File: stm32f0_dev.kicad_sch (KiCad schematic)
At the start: 29 parts, among them U1 STM32F030K6Tx, U2 AP2112K-3.3

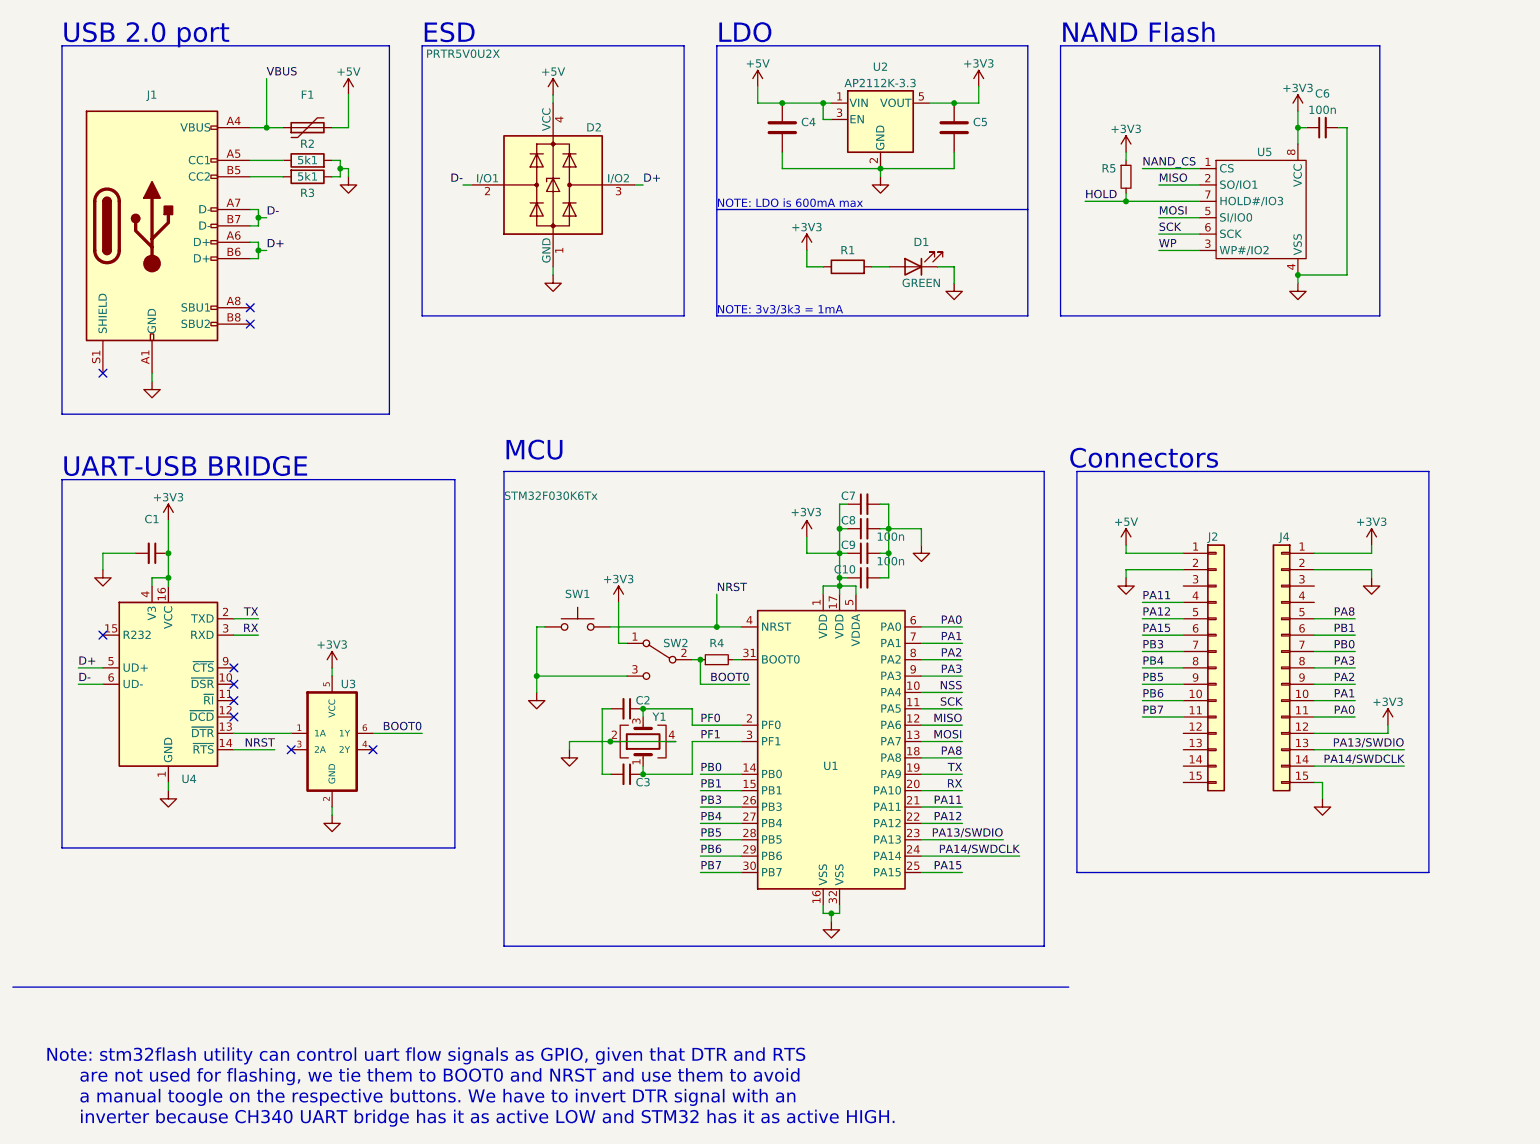
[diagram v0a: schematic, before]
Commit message: Schematic done, routing done, to fix issues on board
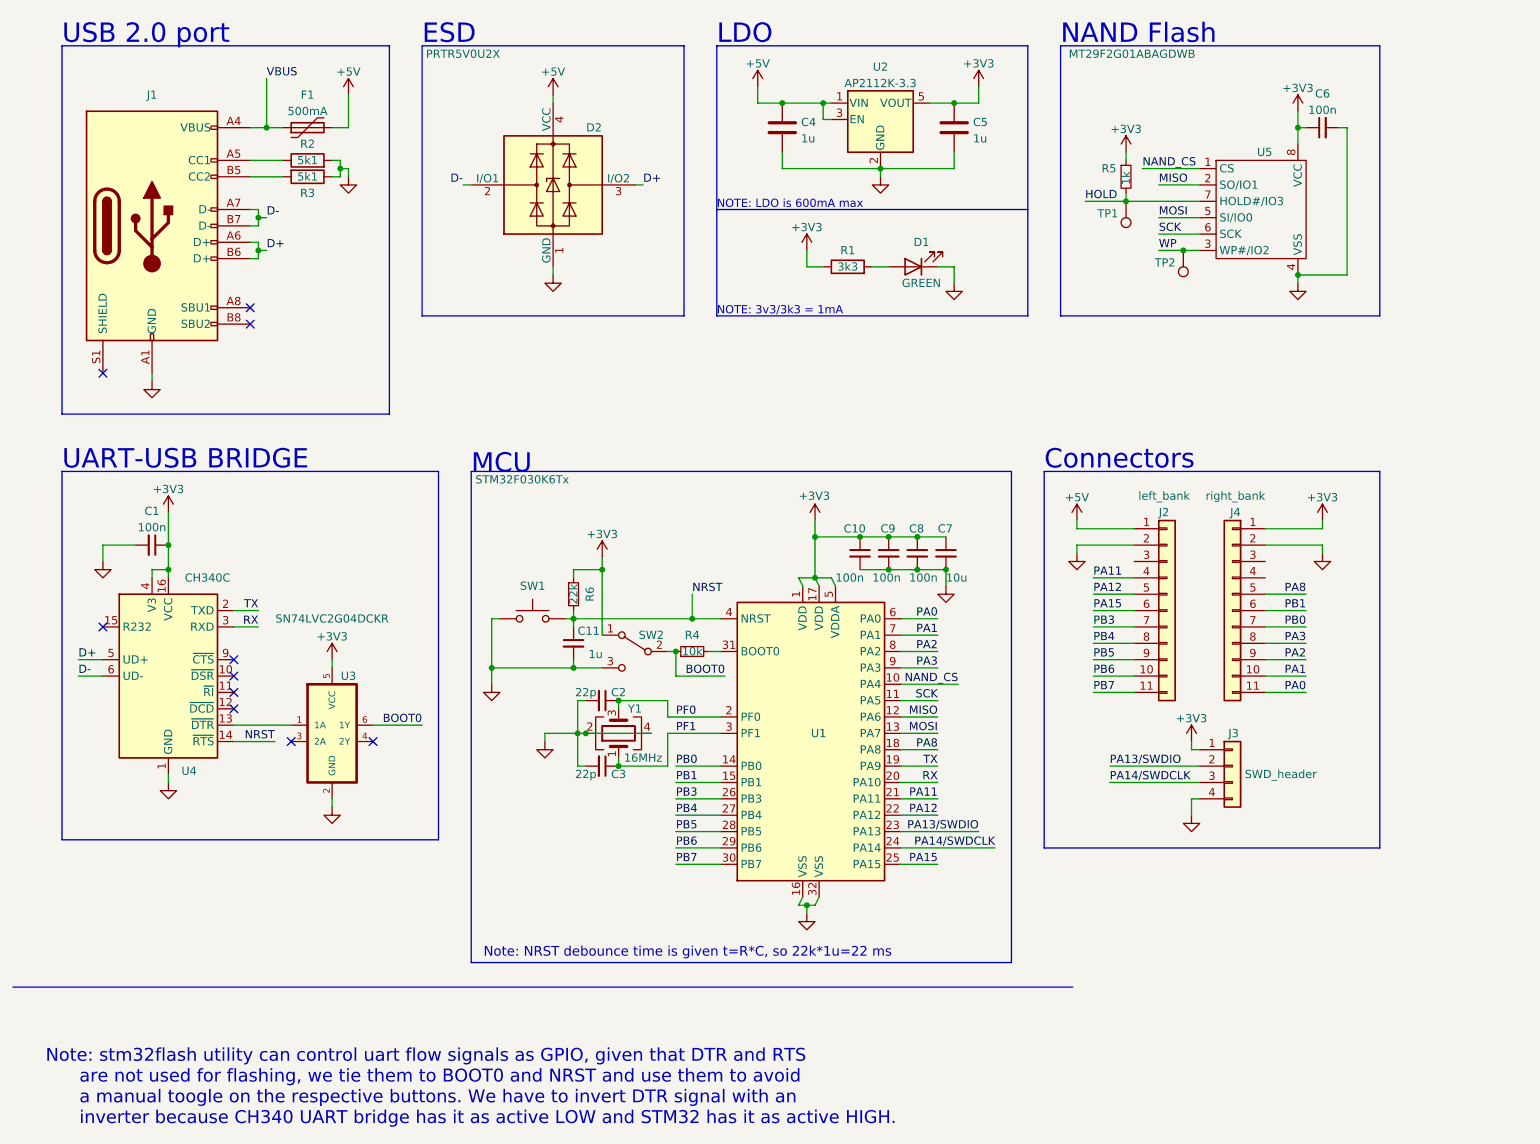
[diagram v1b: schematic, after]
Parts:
- removed J2, J4: (no value), symbol Connector_Generic:Conn_01x15
- added C11: 1u, Capacitor_SMD:C_0603_1608Metric, symbol Device:C_Small
- added J2: left_bank, Connector_PinHeader_2.54mm:PinHeader_1x11_P2.54mm_Vertical, symbol Connector_Generic:Conn_01x11
- added J3: SWD_header, Connector_PinHeader_2.54mm:PinHeader_1x04_P2.54mm_Vertical, symbol Connector_Generic:Conn_01x04
- added J4: right_bank, Connector_PinHeader_2.54mm:PinHeader_1x11_P2.54mm_Vertical, symbol Connector_Generic:Conn_01x11
- added R6: 22k, Resistor_SMD:R_0603_1608Metric, symbol Device:R_Small
- added TP1, TP2: TestPoint, TestPoint:TestPoint_Pad_D1.0mm, symbol Connector:TestPoint
- C1, C10: value (none) -> 100n; footprint (none) -> Capacitor_SMD:C_0603_1608Metric
- C2, C3: value (none) -> 22p; footprint (none) -> Capacitor_SMD:C_0603_1608Metric
- C4, C5: value (none) -> 1u; footprint (none) -> Capacitor_SMD:C_0603_1608Metric
- C6, C8, C9: footprint (none) -> Capacitor_SMD:C_0603_1608Metric
- C7: value (none) -> 10u; footprint (none) -> Capacitor_SMD:C_0603_1608Metric
- D1: footprint (none) -> LED_SMD:LED_0603_1608Metric
- F1: value (none) -> 500mA; footprint (none) -> Fuse:Fuse_0603_1608Metric
- J1: value (none) -> USB_C_Receptacle_USB2.0; footprint (none) -> Connector_USB:USB_C_Receptacle_HRO_TYPE-C-31-M-12
- R1: value (none) -> 3k3; footprint (none) -> Resistor_SMD:R_0603_1608Metric
- R2, R3: footprint (none) -> Resistor_SMD:R_0603_1608Metric
- R4: value (none) -> 10k; footprint (none) -> Resistor_SMD:R_0603_1608Metric
- R5: value (none) -> 1k; footprint (none) -> Resistor_SMD:R_0603_1608Metric
- SW1: value (none) -> SW_Push; footprint (none) -> SKRPACE010:SW_SKRPACE010
- SW2: value (none) -> SW_SPDT; footprint (none) -> SSSS811101 :SSSS811101
- U3: value (none) -> SN74LVC2G04DCKR; footprint (none) -> SN74LVC2G04DCKR:SOT65P210X110-6N
- U4: value (none) -> CH340C; footprint (none) -> Package_SO:SOIC-16_3.9x9.9mm_P1.27mm
- U5: value (none) -> MT29F2G01ABAGDWB; footprint (none) -> MT29F2G01ABAGDWB:SON127P600X800X65-8N
- Y1: value (none) -> 16MHz; footprint (none) -> Crystal:Crystal_SMD_2016-4Pin_2.0x1.6mm
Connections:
- net NSS is gone; now on net NAND_CS: U1.10 (PA4)
- net +3V3: now also J3.1 (Pin_1), J4.1 (Pin_1), R6.1
- net +5V: now also J2.1 (Pin_1)
- net GND: now also C2.2, C3.2, C11.2, J2.2 (Pin_2), J3.4 (Pin_4), J4.2 (Pin_2)
- net HOLD: now also TP1.1
- net NRST: now also C11.1, R6.2
- net PA0: now also J4.11 (Pin_11)
- net PA1: now also J4.10 (Pin_10)
- net PA11: now also J2.4 (Pin_4)
- net PA12: now also J2.5 (Pin_5)
- net PA13/SWDIO: now also J3.2 (Pin_2)
- net PA14/SWDCLK: now also J3.3 (Pin_3)
- net PA15: now also J2.6 (Pin_6)
- net PA2: now also J4.9 (Pin_9)
- net PA3: now also J4.8 (Pin_8)
- net PA8: now also J4.5 (Pin_5)
- net PB0: now also J4.7 (Pin_7)
- net PB1: now also J4.6 (Pin_6)
- net PB3: now also J2.7 (Pin_7)
- net PB4: now also J2.8 (Pin_8)
- net PB5: now also J2.9 (Pin_9)
- net PB6: now also J2.10 (Pin_10)
- net PB7: now also J2.11 (Pin_11)
- net WP: now also TP2.1
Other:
- note added: "Note: NRST debounce time is given t=R*C, so 22k*1u=22 ms"
- moved on the sheet: C1, C10, C2, C3, C7, C8, C9, R4, SW1, SW2, U1, U3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

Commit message: Finished board, added gerber folder, uart leds, board dimensions
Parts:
- added D3, D4: RED, LED_SMD:LED_0603_1608Metric, symbol Device:LED
- added R7, R8: 3k3, Resistor_SMD:R_0603_1608Metric, symbol Device:R
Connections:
- net +3V3: now also R7.1, R8.1
- net RX: now also U4.2 (TXD), D4.1 (K); no longer U4.3 (RXD)
- net TX: now also U4.3 (RXD), D3.1 (K); no longer U4.2 (TXD)
- new net: D4.2 (A), R8.2
- new net: D3.2 (A), R7.2
- no-connect marks 10 -> 13
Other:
- note added: "Note: RX and TX signals are named in respect to mcu, so must be swapped here"
- note added: "Note: stm32flash utility can control uart flow signals as GPIO, given that DTR and RTS are not used for flashing, we tie them to BOOT0 and NRST and use them to avoid manually actuating them for flashing. We have to invert DTR signal with an because CH340 UART bridge has it as active LOW and STM32 has it as active HIGH."
- note added: "Status LEDs"
- note removed: "Note: stm32flash utility can control uart flow signals as GPIO, given that DTR and RTS are not used for flashing, we tie them to BOOT0 and NRST and use them to avoid a manual toogle on the respective buttons. We have to invert DTR signal with an inverter because CH340 UART bridge has it as active LOW and STM32 has it as active HIGH."
- moved on the sheet: C4, C5, C6, D1, R1, R4, R5, TP1, TP2, U2, U5

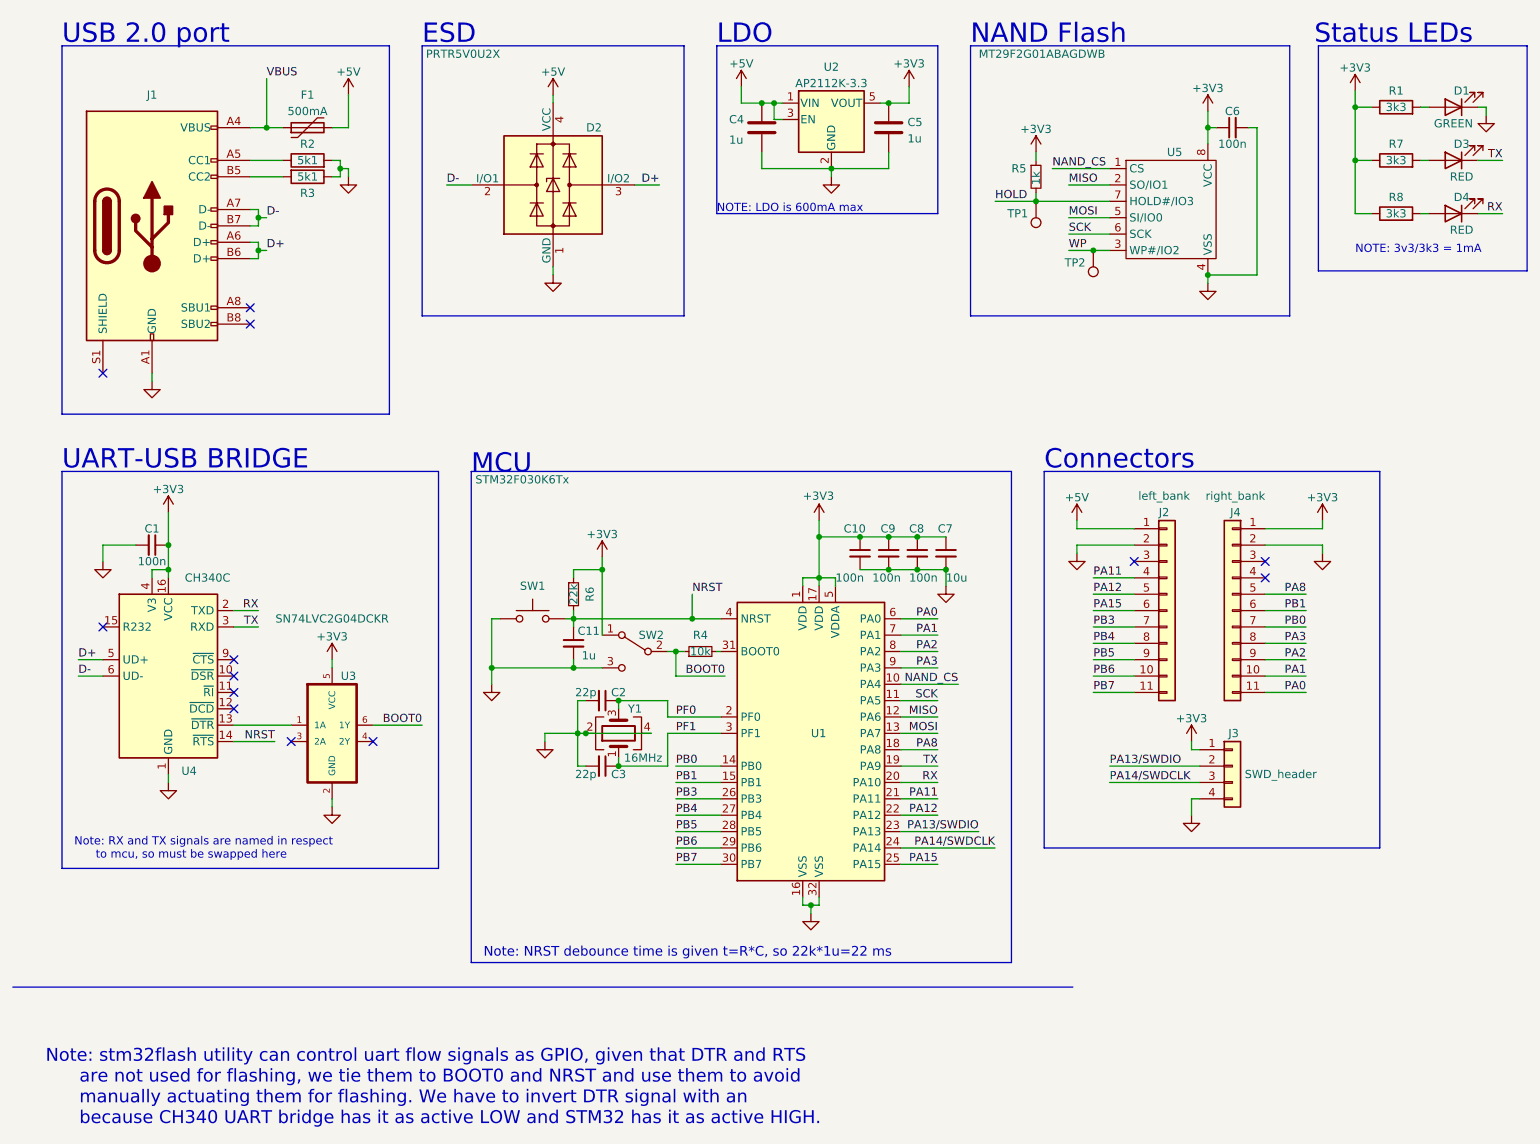
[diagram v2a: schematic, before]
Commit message: Fixed nrst button, dtr signal
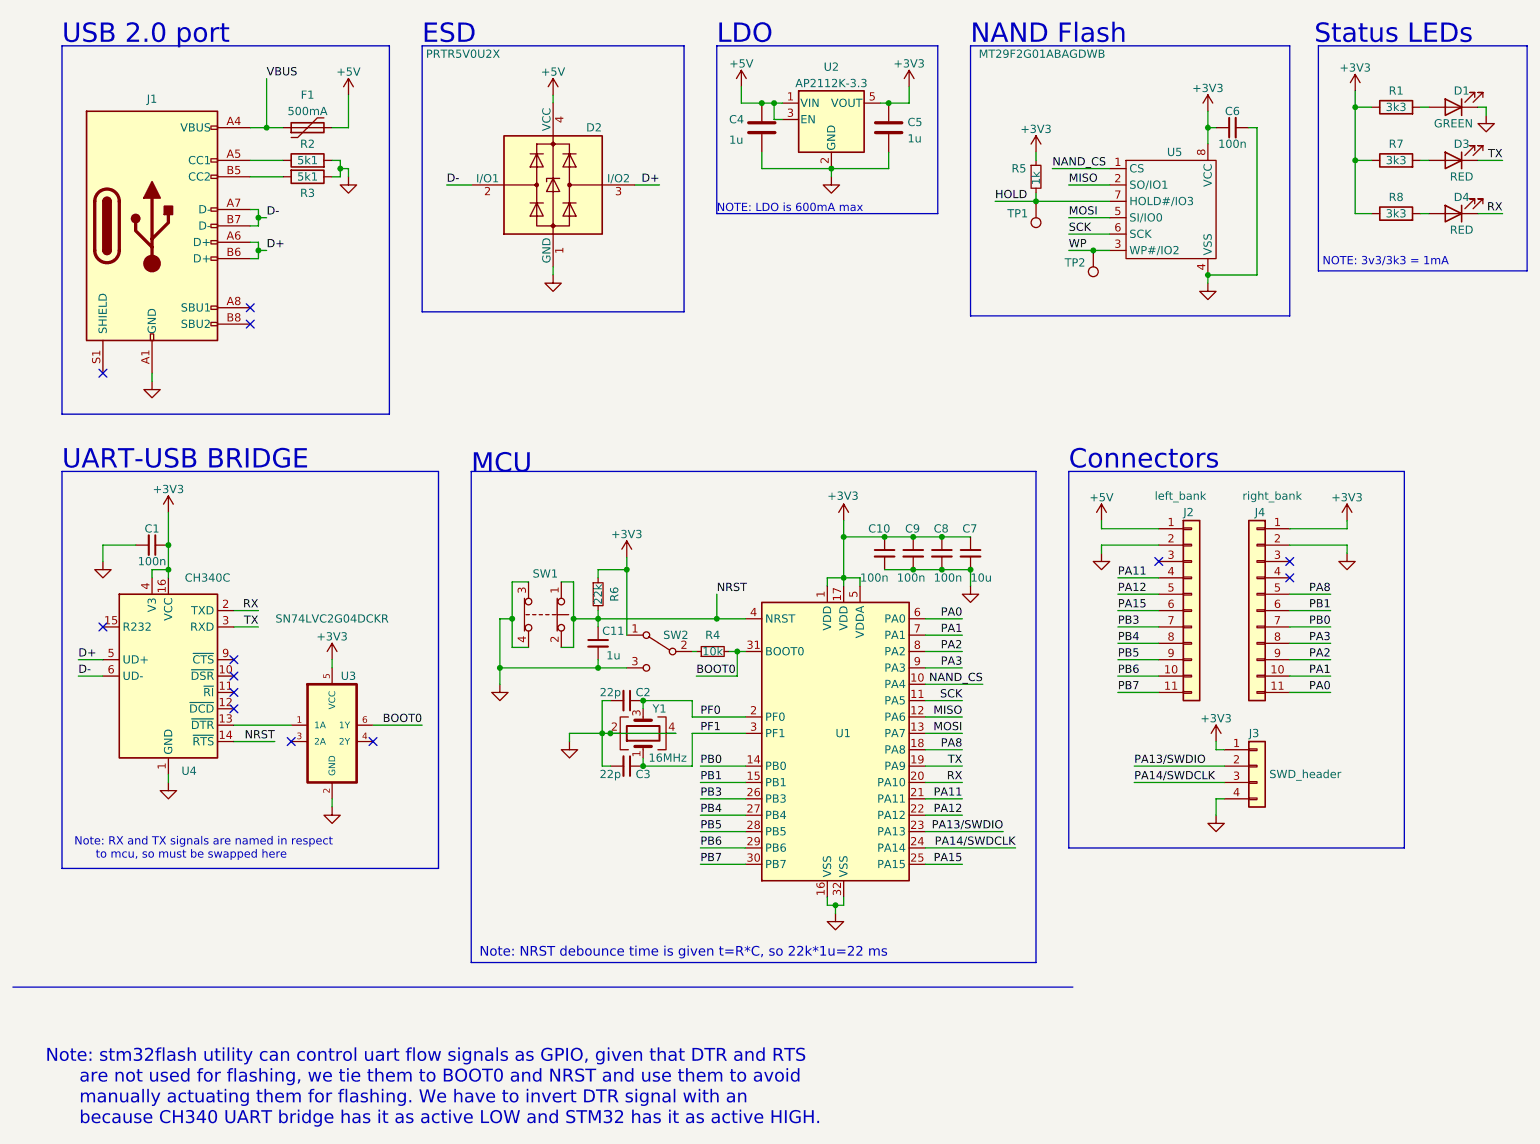
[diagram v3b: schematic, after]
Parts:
- removed SW1: SW_Push, SKRPACE010:SW_SKRPACE010, symbol Switch:SW_Push
- added SW1: SW_Push_Open_Dual, SKRPACE010:SW_SKRPACE010, symbol Switch:SW_Push_Open_Dual
- U1: value STM32F030K6Tx -> (none)
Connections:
- net BOOT0: now also R4.2, U1.31 (BOOT0); no longer R4.1, SW2.2 (B)
- net GND: now also SW1.3, SW1.4
- net NRST: now also SW1.1, SW1.2
- new net: R4.1, SW2.2 (B)
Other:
- moved on the sheet: C10, C11, C2, C3, C7, C8, C9, J2, J3, J4, R4, R6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
